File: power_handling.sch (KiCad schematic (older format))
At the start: 50 parts, among them J1 Power In, U1 LM27762, U11 ADG734, U12 LM1085-5V, U13 ADG734, U14 ADG734, U15 LM27762, U16 ADG734, U17 74ACT32, U2 ADG715, U26 74ACT32, U3 LMZ34002, U4 ADG715, U6 LM1085-12V, U7 TS12A44514, U8 TS12A44514, U9 ADG715

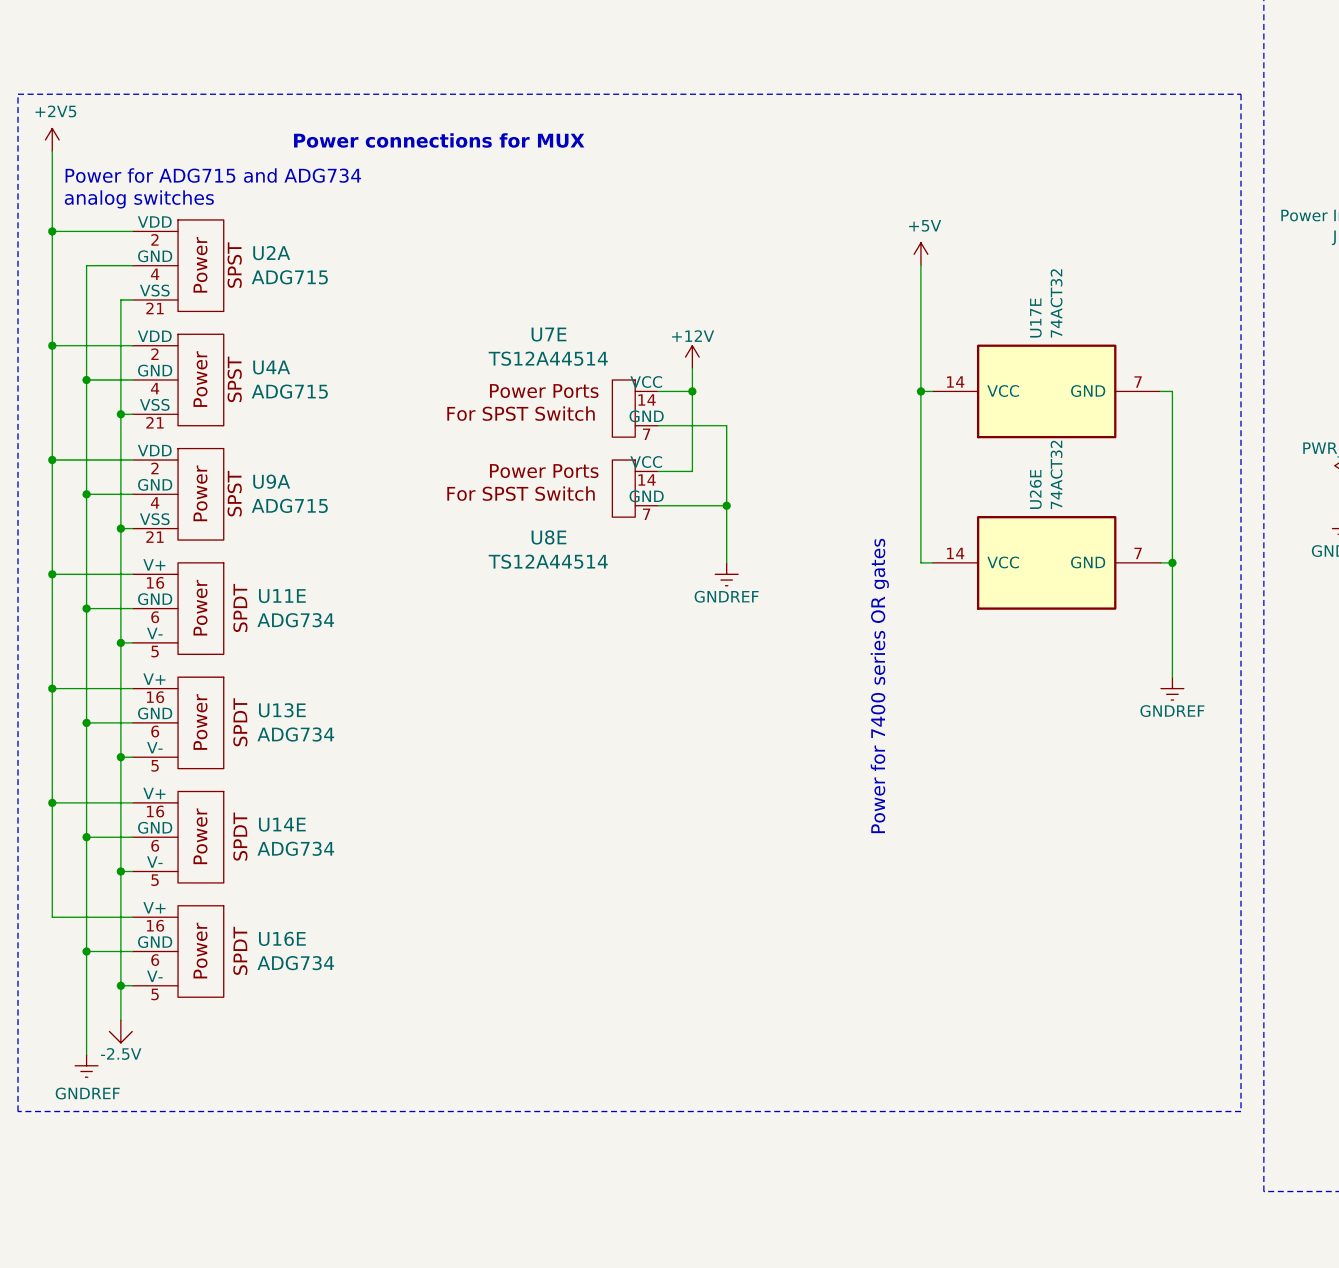
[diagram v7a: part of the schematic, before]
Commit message: Added forgotten bypass caps
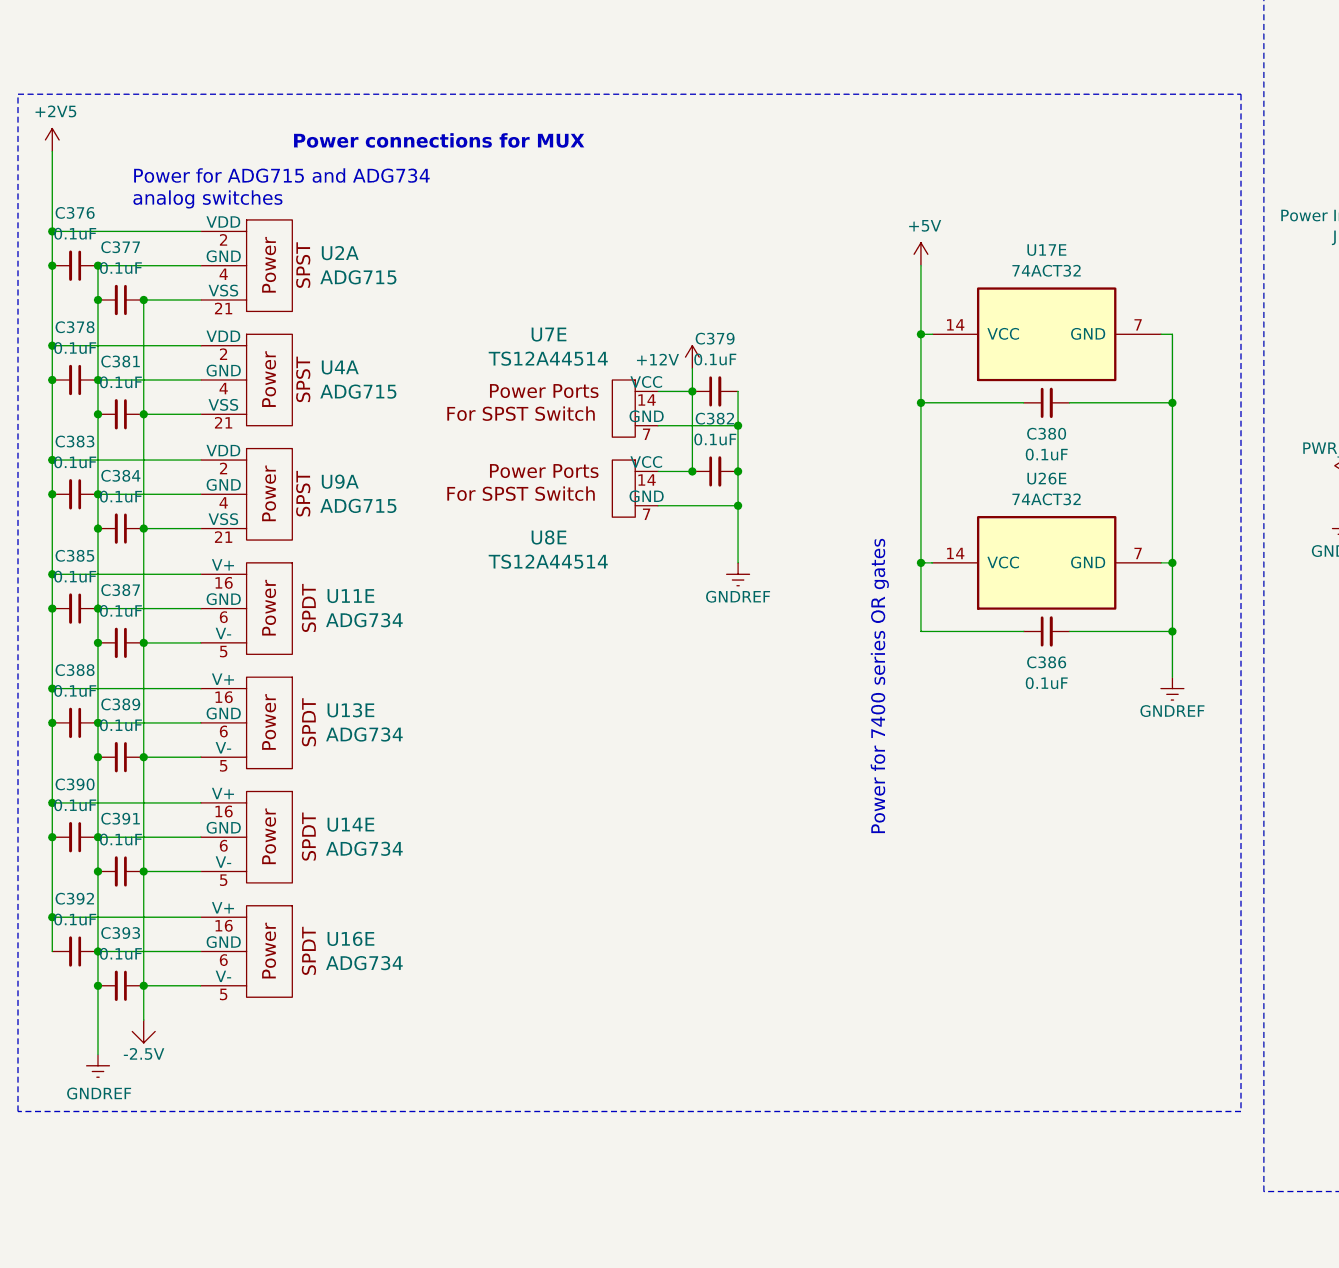
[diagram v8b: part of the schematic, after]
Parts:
- added C376, C377, C378, C379, C380, C381, C382, C383, C384, C385, C386, C387, C388, C389, C390, C391, C392, C393: 0.1uF, Capacitor_SMD:C_0805_2012Metric_Pad1.15x1.50mm_HandSolder, symbol Device:C_Small
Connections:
- net +12V: now also C379.1, C382.1
- net +2V5: now also C376.2, C378.2, C383.2, C385.2, C388.2, C390.2, C392.2
- net +5V: now also C380.1, C386.1
- net -2.5V: now also C377.1, C381.1, C384.1, C387.1, C389.1, C391.1, C393.1
- net GNDREF: now also C376.1, C377.2, C378.1, C379.2, C380.2, C381.2, C382.2, C383.1, C384.2, C385.1, C386.2, C387.2, C388.1, C389.2, C390.1, C391.2, C392.1, C393.2
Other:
- moved on the sheet: U11E, U13E, U14E, U16E, U17E, U2A, U4A, U9A
